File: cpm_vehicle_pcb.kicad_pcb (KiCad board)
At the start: 2 copper layers, 1 part

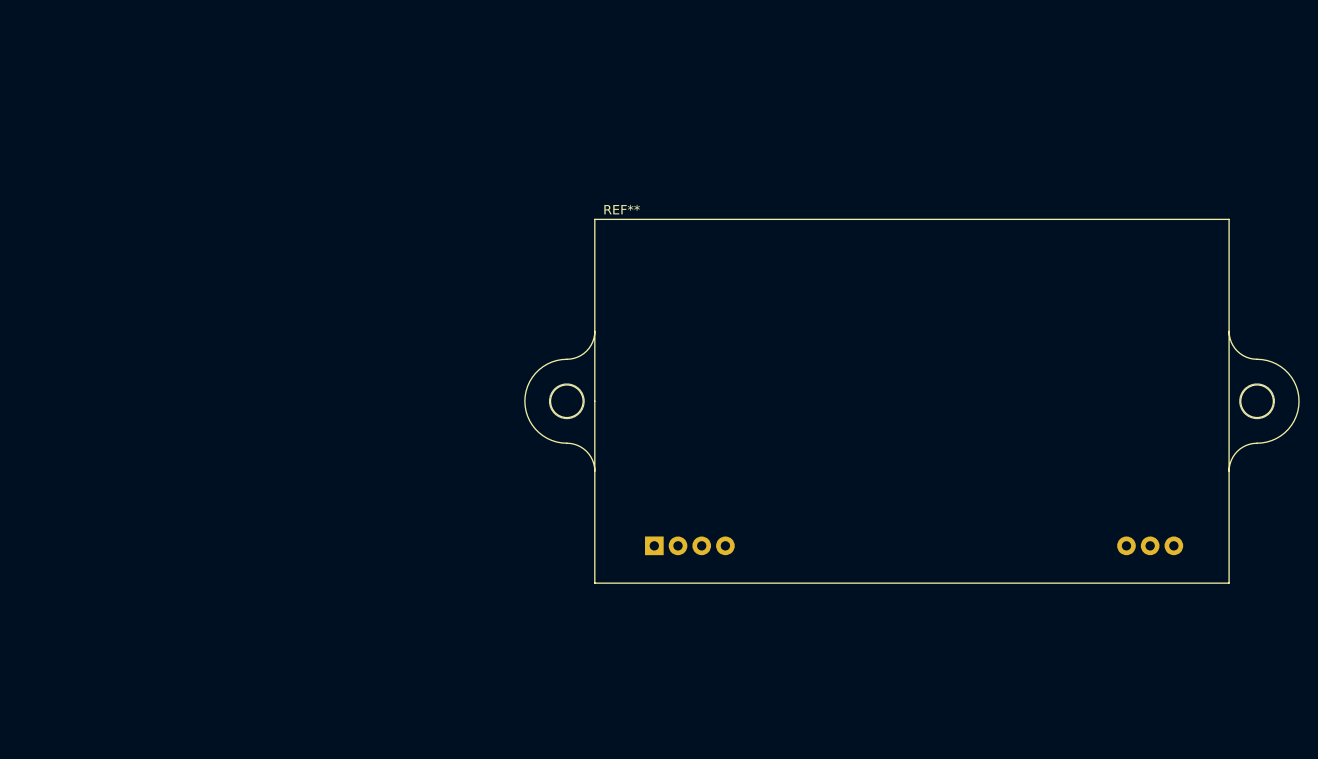
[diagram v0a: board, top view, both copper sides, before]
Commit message: Small footprint changes
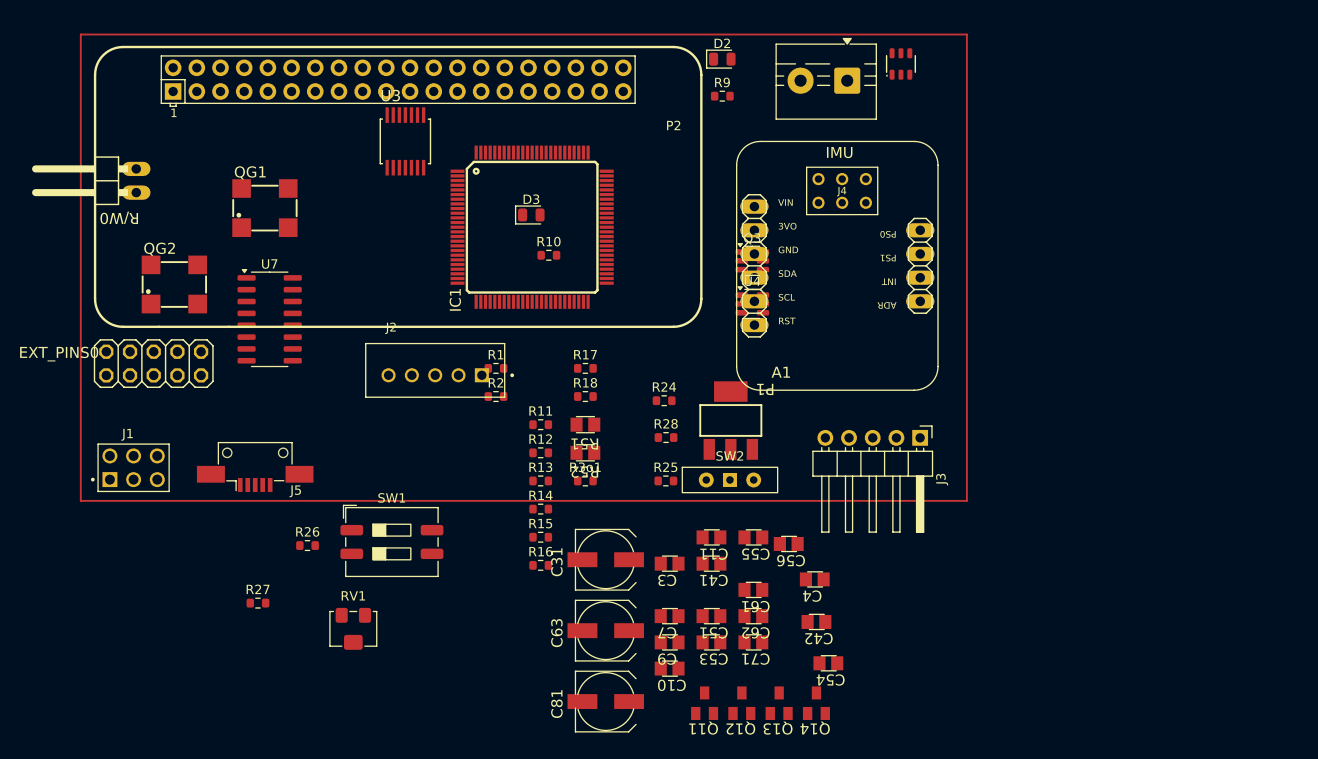
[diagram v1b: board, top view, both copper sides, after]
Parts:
- removed REF**: Reverb_BTDR-1H, Audio_Module:Reverb_BTDR-1H
- added A1: BNO055, footprints_vehicle_pcb:BNO055_IMU, F.Cu at (173.1, 66.8)
- added C10: 10nF, footprints_vehicle_pcb:C0805_10681391, F.Cu at (155.1, 110.0)
- added C11: 100nF, footprints_vehicle_pcb:C0805_10681391, F.Cu at (159.6, 95.9)
- added C3: 10uF, footprints_vehicle_pcb:C0805_10681391, F.Cu at (155.1, 98.7)
- added C31: 220uF, footprints_vehicle_pcb:UD-6,3X5,8_Electrolytic_CAP, F.Cu at (148.3, 98.3)
- added C4: 220uF, footprints_vehicle_pcb:C0805_10681391, F.Cu at (170.7, 100.4)
- added C41: 100nF, footprints_vehicle_pcb:C0805_10681391, F.Cu at (159.6, 98.7)
- added C42: 100nF, footprints_vehicle_pcb:C0805_10681391, F.Cu at (170.9, 105.0)
- added C51: 100nF, footprints_vehicle_pcb:C0805_10681391, F.Cu at (159.6, 104.4)
- added C53: 100nF, footprints_vehicle_pcb:C0805_10681391, F.Cu at (159.6, 107.2)
- added C54: 100nF, footprints_vehicle_pcb:C0805_10681391, F.Cu at (172.2, 109.4)
- added C55: 100nF, footprints_vehicle_pcb:C0805_10681391, F.Cu at (164.1, 95.9)
- added C56: 100nF, footprints_vehicle_pcb:C0805_10681391, F.Cu at (167.9, 96.6)
- added C61: 100nF, footprints_vehicle_pcb:C0805_10681391, F.Cu at (164.1, 101.5)
- added C62: 100nF, footprints_vehicle_pcb:C0805_10681391, F.Cu at (164.1, 104.4)
- added C63: 220uF, footprints_vehicle_pcb:UD-6,3X5,8_Electrolytic_CAP, F.Cu at (148.3, 105.9)
- added C7: 220uF, footprints_vehicle_pcb:C0805_10681391, F.Cu at (155.1, 104.4)
- added C71: 10nF, footprints_vehicle_pcb:C0805_10681391, F.Cu at (164.1, 107.2)
- added C81: 220uF, footprints_vehicle_pcb:UD-6,3X5,8_Electrolytic_CAP, F.Cu at (148.3, 113.5)
- added C9: 100nF, footprints_vehicle_pcb:C0805_10681391, F.Cu at (155.1, 107.2)
- added D2: LED, LED_SMD:LED_0805_2012Metric, F.Cu at (160.8, 44.6)
- added D3: LED, LED_SMD:LED_0805_2012Metric, F.Cu at (140.3, 61.4)
- added EXT_PINS0: PINHD-2X5, footprints_vehicle_pcb:2X05_EXT_PINS, F.Cu at (99.8, 77.3)
- added IC1: ATMEGAAU, footprints_vehicle_pcb:TQFP100_atmega2560, F.Cu at (140.4, 62.7)
- added IC2: RPI-ZERO, footprints_vehicle_pcb:rpi_zero_w, F.Cu at (93.5, 73.3)
- added J1: Conn_02x03_Counter_Clockwise, footprints_vehicle_pcb:HARWIN_M20-9980346, F.Cu at (97.7, 88.5)
- added J2: Conn_02x03_Counter_Clockwise, footprints_vehicle_pcb:JST_B5B-XH-A, F.Cu at (130.0, 78.0)
- added J3: Conn_01x05, footprints_vehicle_pcb:PinHeader_1x05_P2.54mm_Horizontal, F.Cu at (182.0, 85.2)
- added J4: AVR-ISP-6, footprints_vehicle_pcb:AVR_ISP_6_footprint, F.Cu at (173.6, 58.8)
- added J5: USB_B_Mini, Connector_USB:USB_Mini-B_AdamTech_MUSB-B5-S-VT-TSMT-1_SMD_Vertical, F.Cu at (110.7, 88.7)
- added P1: NCP1117, footprints_vehicle_pcb:SOT223_ncp1117, F.Cu at (161.7, 83.4)
- added P2: OSTTE020104, TerminalBlock:TerminalBlock_MaiXu_MX126-5.0-02P_1x02_P5.00mm, F.Cu at (174.2, 47.0)
- added Q11: BSS123, footprints_vehicle_pcb:SOT23_NMOS, F.Cu at (158.9, 113.7)
- added Q12: BSS123, footprints_vehicle_pcb:SOT23_NMOS, F.Cu at (162.9, 113.7)
- added Q13: BSS123, footprints_vehicle_pcb:SOT23_NMOS, F.Cu at (166.9, 113.7)
- added Q14: BSS123, footprints_vehicle_pcb:SOT23_NMOS, F.Cu at (170.9, 113.7)
- added Q3: DMG9926UDM, Package_TO_SOT_SMD:SOT-23-6, F.Cu at (164.0, 66.3)
- added QG1: XO91, footprints_vehicle_pcb:SM77H_crystal_oscillator, F.Cu at (111.7, 60.6)
- added QG2: XO91, footprints_vehicle_pcb:SM77H_crystal_oscillator, F.Cu at (102.0, 68.8)
- added R/W0: PINHD-1X2/90, footprints_vehicle_pcb:1X02_90_rpi, F.Cu at (94.1, 57.7)
- added R1: 1K, Resistor_SMD:R_0603_1608Metric, F.Cu at (136.5, 77.8)
- added R10: 330, Resistor_SMD:R_0603_1608Metric, F.Cu at (142.2, 65.7)
- added R11: 180, Resistor_SMD:R_0603_1608Metric, F.Cu at (141.3, 83.8)
- added R12: 180, Resistor_SMD:R_0603_1608Metric, F.Cu at (141.3, 86.8)
- added R13: 180, Resistor_SMD:R_0603_1608Metric, F.Cu at (141.3, 89.9)
- added R14: 180, Resistor_SMD:R_0603_1608Metric, F.Cu at (141.3, 92.9)
- added R15: 330, Resistor_SMD:R_0603_1608Metric, F.Cu at (141.3, 95.9)
- added R16: 330, Resistor_SMD:R_0603_1608Metric, F.Cu at (141.3, 98.9)
- added R17: 330, Resistor_SMD:R_0603_1608Metric, F.Cu at (146.1, 77.8)
- added R18: 330, Resistor_SMD:R_0603_1608Metric, F.Cu at (146.1, 80.8)
- added R2: 1K, Resistor_SMD:R_0603_1608Metric, F.Cu at (136.5, 80.8)
- added R24: 1K, Resistor_SMD:R_0603_1608Metric, F.Cu at (154.5, 81.3)
- added R25: 330, Resistor_SMD:R_0603_1608Metric, F.Cu at (154.7, 89.9)
- added R26: 1k, Resistor_SMD:R_0603_1608Metric, F.Cu at (116.3, 96.8)
- added R27: 1k, Resistor_SMD:R_0603_1608Metric, F.Cu at (111.0, 103.0)
- added R28: 330, Resistor_SMD:R_0603_1608Metric, F.Cu at (154.7, 85.2)
- added R3o1: 1K, Resistor_SMD:R_0603_1608Metric, F.Cu at (146.1, 89.9)
- added R51: 10k 0,1%, footprints_vehicle_pcb:R0805_10681391, F.Cu at (146.1, 83.8)
- added R52: 1k 0,1%, footprints_vehicle_pcb:R0805_10681391, F.Cu at (146.1, 86.8)
- added R9: 330, Resistor_SMD:R_0603_1608Metric, F.Cu at (160.8, 48.6)
- added RV1: R_Potentiometer, Potentiometer_SMD:Potentiometer_Bourns_3214W_Vertical, F.Cu at (121.2, 105.7)
- added SW1: SW_DIP_x02, Button_Switch_SMD:SW_DIP_SPSTx02_Slide_9.78x7.26mm_W8.61mm_P2.54mm, F.Cu at (125.4, 96.4)
- added SW2: SW_SPDT_312, Button_Switch_THT:SW_Slide-03_Wuerth-WS-SLTV_10x2.5x6.4_P2.54mm, F.Cu at (161.6, 89.8)
- added U3: TXB0104PWR, footprints_vehicle_pcb:TXB0104PWR, F.Cu at (126.8, 53.5)
- added U4: MT3608, Package_TO_SOT_SMD:SOT-23-6, F.Cu at (164.0, 70.9)
- added U7: CH340G, Package_SO:SOIC-16_3.9x9.9mm_P1.27mm, F.Cu at (112.2, 72.5)
- added U8: R5460N, PCM_JLCPCB:SOT-23-6_L2.9-W1.6-P0.95-LS2.8-BL, F.Cu at (179.9, 45.2)

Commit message: update
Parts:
- added D4: D_Schottky, Capacitor_THT:CP_Radial_D4.0mm_P1.50mm, F.Cu at (186.0, 100.4)
- C31: footprint footprints_vehicle_pcb:UD-6,3X5,8_Electrolytic_CAP -> Capacitor_THT:CP_Radial_D6.3mm_P2.50mm
- moved SW1 33.0 mm to (123.5, 63.5)
- moved C31 14.2 mm to (137.0, 107.0)

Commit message: some minute changes
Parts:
- removed C81: 220uF, footprints_vehicle_pcb:UD-6,3X5,8_Electrolytic_CAP
- removed D4: D_Schottky, Capacitor_THT:CP_Radial_D4.0mm_P1.50mm
- removed J4: AVR-ISP-6, footprints_vehicle_pcb:AVR_ISP_6_footprint
- removed P2: OSTTE020104, TerminalBlock:TerminalBlock_MaiXu_MX126-5.0-02P_1x02_P5.00mm
- added D1: SS54, PCM_JLCPCB:D_SMA, F.Cu at (170.8, 53.3)
- added D6: SS54, PCM_JLCPCB:D_SMA, F.Cu at (173.1, 61.3)
- added J6: Conn_01x03_Socket, Connector_PinSocket_2.54mm:PinSocket_1x03_P2.54mm_Horizontal, F.Cu at (178.5, 90.2)
- added R21: 3.3K, Resistor_SMD:R_0603_1608Metric, F.Cu at (175.5, 56.4)
- C31: footprint Capacitor_THT:CP_Radial_D6.3mm_P2.50mm -> footprints_vehicle_pcb:C0805_10681391
- C4, C7: value 220uF -> 22uF; footprint footprints_vehicle_pcb:C0805_10681391 -> Capacitor_SMD:C_0603_1608Metric
- C63: footprint footprints_vehicle_pcb:UD-6,3X5,8_Electrolytic_CAP -> footprints_vehicle_pcb:C0805_10681391
- J2: footprint footprints_vehicle_pcb:JST_B5B-XH-A -> footprints_vehicle_pcb:HARWIN_M20-9980346
- R51, R52: footprint footprints_vehicle_pcb:R0805_10681391 -> Resistor_SMD:R_0603_1608Metric
- moved Q13 71.3 mm to (131.1, 52.0)
- moved Q14 71.0 mm to (136.9, 51.3)
- moved Q12 68.4 mm to (127.7, 55.0)
- moved C31 64.8 mm to (105.9, 50.2)
- moved Q11 62.7 mm to (126.6, 59.9)
- moved C51 60.1 mm to (133.6, 50.1)
- moved C42 59.3 mm to (130.0, 62.0)
- moved R16 52.9 mm to (121.9, 49.7)
- moved C10 51.5 mm to (116.1, 76.4)
- moved C54 50.8 mm to (153.5, 62.1)
- moved C53 50.5 mm to (153.3, 57.1)
- moved C4 48.9 mm to (176.4, 51.9)
- moved R15 47.0 mm to (128.1, 50.8)
- moved RV1 46.1 mm to (159.8, 80.5)
- moved C71 45.6 mm to (131.8, 75.0)
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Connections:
- net /R17 renamed Net-(Q13-D)
- net /R18 renamed Net-(Q14-D)
- C11 pad 2: GND_battery -> B-
- C3 pad 1: +7.5V -> +8.5V
- C3 pad 2: GND_battery -> GND
- C31 pad 1: (no net) -> +5V
- C31 pad 2: (no net) -> GND
- C4 pad 2: GND_battery -> GND
- C7 pad 1: GND_battery -> GND
- C9 pad 2: GND_battery -> B-
- IC1 pad 7: unconnected-(IC1-(OC3C/INT5)PE5-Pad7) -> /SERVO_PWM
- IC1 pad 90: /TDI -> unconnected-(IC1-(ADC7/TDI)PF7-Pad90)
- IC1 pad 91: /TDO -> unconnected-(IC1-(ADC6/TDO)PF6-Pad91)
- IC1 pad 92: /TMS -> unconnected-(IC1-(ADC5/TMS)PF5-Pad92)
- IC1 pad 93: /TCK -> unconnected-(IC1-(ADC4/TCK)PF4-Pad93)
- Q3 pad 3: GND_battery -> B-
- R25 pad 1: vcc_bat -> B+
- R51 pad 2: /VCC_BAT -> vcc_bat
- SW2 pad 1: unconnected-(SW2-B-Pad1) -> B+
- SW2 pad 2: +7.5V -> vcc_bat
- SW2 pad 3: vcc_bat -> +8.5V
- U4 pad 2: GND_battery -> GND
- U8 pad 6: GND_battery -> B-
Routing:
- added copper zone on F.Cu, net GND

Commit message: update
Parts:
- added L1: 20uH, Inductor_SMD:L_10.4x10.4_H4.8, F.Cu at (173.0, 60.8)
- added R3: 10k, Resistor_SMD:R_0603_1608Metric, F.Cu at (146.4, 80.0)
- added R4: 10k, Resistor_SMD:R_0603_1608Metric, F.Cu at (146.4, 82.5)
- R26, R27: moved to B.Cu
- moved R21 25.7 mm to (164.2, 79.5)
- moved C4 21.2 mm to (167.7, 71.2)
- moved D6 20.1 mm to (158.0, 74.5)
- moved D1 20.0 mm to (182.5, 69.5)
- moved QG1 17.4 mm to (139.8, 77.5)
- moved C41 13.7 mm to (116.5, 67.0)
- moved QG2 12.7 mm to (114.0, 79.0)
- moved R25 11.3 mm to (185.2, 74.8)
- moved R1 11.0 mm to (138.7, 67.0)
- moved C71 10.8 mm to (139.8, 82.2), turned to 180 degrees
- moved R26 9.42 mm to (125.2, 85.0)
- moved C10 7.33 mm to (114.0, 83.4), turned to 180 degrees
- moved Q3 6.86 mm to (172.5, 84.8)
- moved SW1 6.65 mm to (111.2, 61.5), turned to 180 degrees
- moved R27 5.71 mm to (122.2, 85.0)
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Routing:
- net /TX0: track 0.00 -> 31.9 mm, vias 0 -> 1
- net /SDA: track 0.00 -> 30.2 mm
- net /RX0: track 0.00 -> 29.8 mm, vias 0 -> 1
- net /SCL: track 0.00 -> 29.4 mm
- net /SS_PI: track 0.00 -> 24.9 mm, vias 0 -> 1
- net /SCK_PI: track 0.00 -> 24.2 mm, vias 0 -> 1
- net /MOSI_PI: track 0.00 -> 23.1 mm, vias 0 -> 1
- net Net-(U3-VCCB): track 0.00 -> 17.7 mm
- net +3V3: track 0.00 -> 17.2 mm
- net +5V: track 0.00 -> 14.7 mm
- net Net-(U3-VCCA): track 0.00 -> 14.6 mm
- net Net-(QG2-OUT): track 0.00 -> 14.1 mm
- net /XTAL1: track 0.00 -> 5.35 mm
- net Net-(J5-D-): track 0.00 -> 4.45 mm
- net Net-(J5-D+): track 0.00 -> 4.26 mm
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
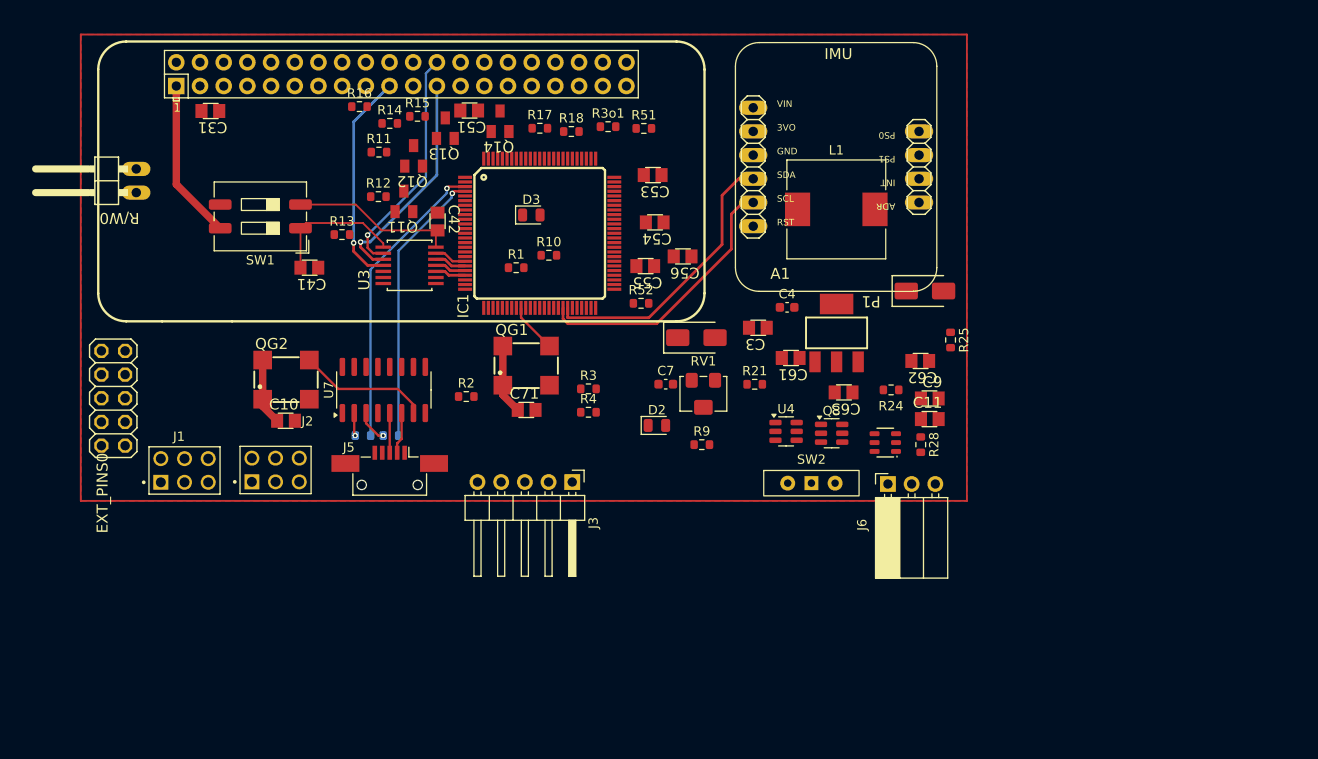
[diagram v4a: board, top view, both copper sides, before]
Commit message: Battery Protection Routing done
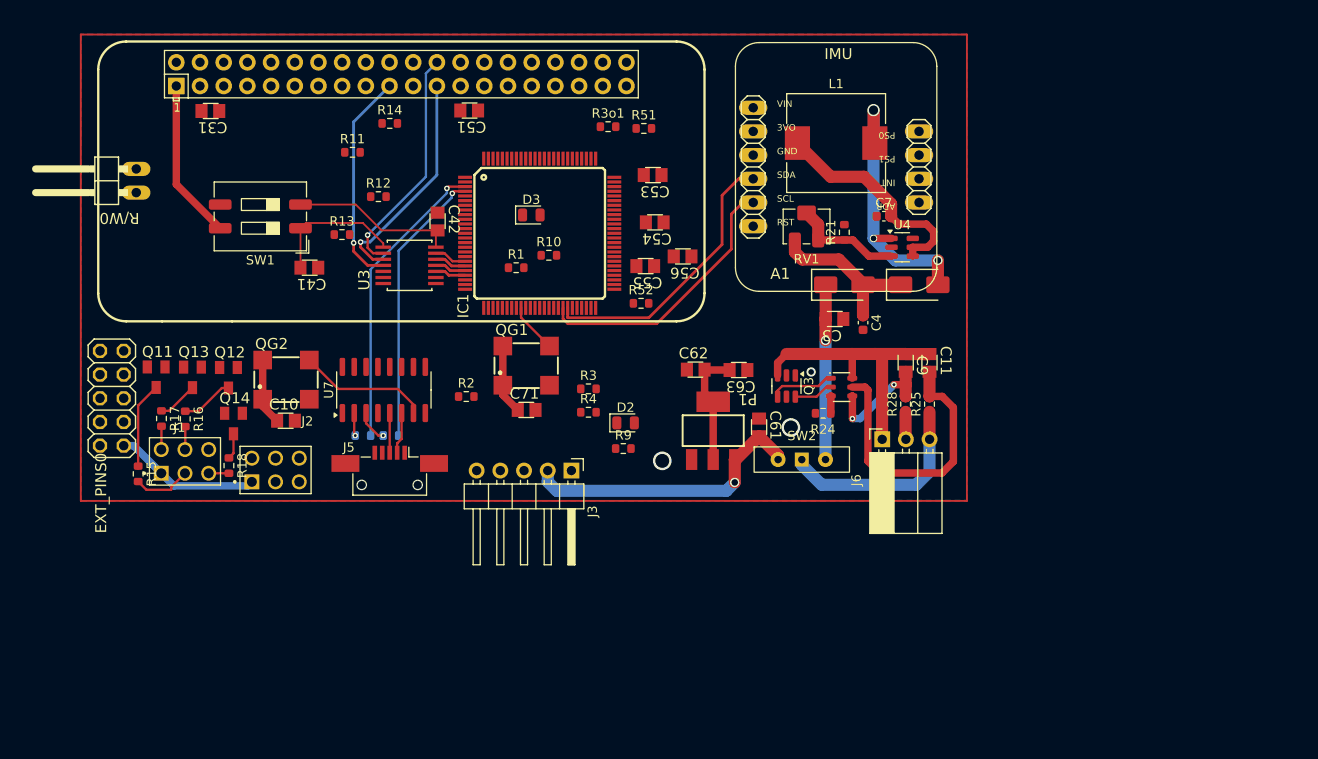
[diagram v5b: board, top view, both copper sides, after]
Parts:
- moved R18 51.3 mm to (107.9, 88.2), turned to -90 degrees
- moved R17 51.1 mm to (100.7, 83.2), turned to -90 degrees
- moved R15 48.6 mm to (98.2, 89.1), turned to -90 degrees
- moved Q14 43.2 mm to (108.4, 83.7), turned to 180 degrees
- moved R16 38.3 mm to (103.2, 83.2), turned to -90 degrees
- moved Q13 38.1 mm to (104.0, 78.8), turned to 180 degrees
- moved Q11 32.6 mm to (100.1, 78.7), turned to 180 degrees
- moved Q12 31.0 mm to (107.8, 78.8), turned to 180 degrees
- moved C7 29.5 mm to (178.1, 61.5)
- moved C62 24.1 mm to (157.9, 77.9), turned to 180 degrees
- moved U4 23.3 mm to (180.1, 64.8)
- moved RV1 21.1 mm to (169.8, 62.6), turned to 180 degrees
- moved R21 18.9 mm to (173.9, 63.2), turned to 90 degrees
- moved P1 16.9 mm to (159.8, 84.5)
- moved D6 16.8 mm to (173.9, 68.8)
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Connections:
- net Net-(Q13-D) renamed /R17
- net Net-(Q14-D) renamed /R18
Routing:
- net vcc_bat: track 0.00 -> 31.5 mm, vias 0 -> 1
- net Net-(U8-VDD): track 0.00 -> 31.1 mm
- net Net-(U4-SW): track 0.00 -> 30.0 mm, vias 0 -> 3
- net B-: track 0.00 -> 29.8 mm
- net +5V: track 14.7 -> 43.1 mm
- net Net-(U4-EN): track 0.00 -> 23.8 mm
- net B+: track 0.00 -> 22.1 mm
- net +8.5V: track 0.00 -> 18.7 mm, vias 0 -> 1
- net Net-(C4-Pad1): track 0.00 -> 17.4 mm
- net Net-(U8-VC): track 0.00 -> 12.3 mm, vias 0 -> 2
- net Net-(U4-FB): track 0.00 -> 12.0 mm
- net /R15: track 0.00 -> 9.25 mm
- net Net-(Q3-G2): track 0.00 -> 6.91 mm
- net /LED1_PIN: track 0.00 -> 6.29 mm
- net /R16: track 0.00 -> 5.66 mm
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- added copper zone on B.Cu, net GND

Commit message: Some Routing
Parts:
- R26, R27: moved to F.Cu
- moved R3o1 46.2 mm to (113.9, 82.5), turned to -90 degrees
- moved R52 33.4 mm to (122.2, 55.8)
- moved R1 25.0 mm to (119.0, 82.5), turned to -90 degrees
- moved C10 24.1 mm to (136.8, 75.6), turned to 0 degrees
- moved R51 23.3 mm to (129.4, 56.3)
- moved C54 23.3 mm to (132.3, 52.4)
- moved QG2 23.1 mm to (137.1, 80.4), turned to 180 degrees
- moved D3 17.0 mm to (130.0, 74.9), turned to -90 degrees
- moved R2 17.0 mm to (116.5, 82.4), turned to -90 degrees
- moved R10 13.8 mm to (132.0, 75.0), turned to 90 degrees
- moved C71 11.0 mm to (150.7, 80.8), turned to -90 degrees
- moved C56 10.7 mm to (166.1, 70.5)
- moved C55 10.2 mm to (161.4, 71.9)
- moved R4 9.62 mm to (143.7, 73.3), turned to -90 degrees
- moved R27 9.57 mm to (125.1, 75.8), turned to 90 degrees
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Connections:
- EXT_PINS0 pad 10: /ERW8 -> /ERW4
- EXT_PINS0 pad 3: /ERW1 -> /ERW5
- EXT_PINS0 pad 4: /ERW5 -> /ERW1
- EXT_PINS0 pad 5: /ERW2 -> /ERW6
- EXT_PINS0 pad 6: /ERW6 -> /ERW2
- EXT_PINS0 pad 7: /ERW3 -> /ERW7
- EXT_PINS0 pad 8: /ERW7 -> /ERW3
- EXT_PINS0 pad 9: /ERW4 -> /ERW8
- IC1 pad 16: /ERW6 -> /LED2
- IC1 pad 17: /LED4 -> /LED3
- IC1 pad 18: /LED3 -> /LED4
- IC1 pad 2: unconnected-(IC1-(RXD0/PCIN8)PE0-Pad2) -> /RX0
- IC1 pad 23: /ERW8 -> /LED1
- IC1 pad 24: /ERW7 -> /SERVO_PWM
- IC1 pad 25: /LED_BUILT_IN -> /PWM
- IC1 pad 26: /LED1 -> /LED_BUILT_IN
- IC1 pad 27: /LED2 -> unconnected-(IC1-PH7(T4)-Pad27)
- IC1 pad 4: /RX0 -> unconnected-(IC1-(XCK0/AIN0)PE2-Pad4)
- IC1 pad 5: unconnected-(IC1-(OC3A/AIN1)PE3-Pad5) -> /ERW8
- IC1 pad 6: unconnected-(IC1-(OC3B/INT4)PE4-Pad6) -> /ERW7
- IC1 pad 7: /SERVO_PWM -> /ERW6
- IC1 pad 71: /ERW1 -> /ERW4
- IC1 pad 72: /ERW2 -> /ERW3
- IC1 pad 73: /ERW3 -> /ERW2
- IC1 pad 74: /ERW4 -> /ERW1
- IC1 pad 8: /PWM -> unconnected-(IC1-(T3/INT6)PE6-Pad8)
- J2 pad 3: /SENSOR1 -> unconnected-(J2-Pin_3-Pad3)
- J2 pad 4: unconnected-(J2-Pin_4-Pad4) -> /SENSOR2
- J2 pad 5: /SENSOR2 -> GND
- J2 pad 6: GND -> /SENSOR1
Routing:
- net /ERW1: track 0.00 -> 92.9 mm, vias 0 -> 1
- net /ERW2: track 0.00 -> 87.7 mm, vias 0 -> 1
- net /ERW3: track 0.00 -> 82.8 mm, vias 0 -> 1
- net /ERW4: track 0.00 -> 76.7 mm, vias 0 -> 1
- net /SENSOR3: track 0.00 -> 47.1 mm, vias 0 -> 2
- net /MISO_PI: track 0.00 -> 45.1 mm
- net /SENSOR2: track 0.00 -> 45.1 mm, vias 0 -> 2
- net /ERW6: track 0.00 -> 45.0 mm, vias 0 -> 1
- net /ERW7: track 0.00 -> 44.4 mm, vias 0 -> 1
- net /SENSOR1: track 0.00 -> 44.0 mm, vias 0 -> 2
- net /ERW8: track 0.00 -> 43.9 mm, vias 0 -> 1
- net /TX0: track 31.9 -> 0.00 mm, vias 1 -> 0
- net /RX0: track 29.8 -> 0.00 mm, vias 1 -> 0
- net +5V: track 43.1 -> 64.1 mm
- net /SS_PI: track 24.9 -> 45.4 mm, vias 1 -> 0
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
